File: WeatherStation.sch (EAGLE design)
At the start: 35 parts, among them J1 EDISON_CONNECTOR_FULLMOUNTING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, J2 EDISON_CONNECTOR_FULLHEADER, U1 MCP73831, U2 HTU21DSMD, U3 MPL3115A2LGA8, U4 PCA9306

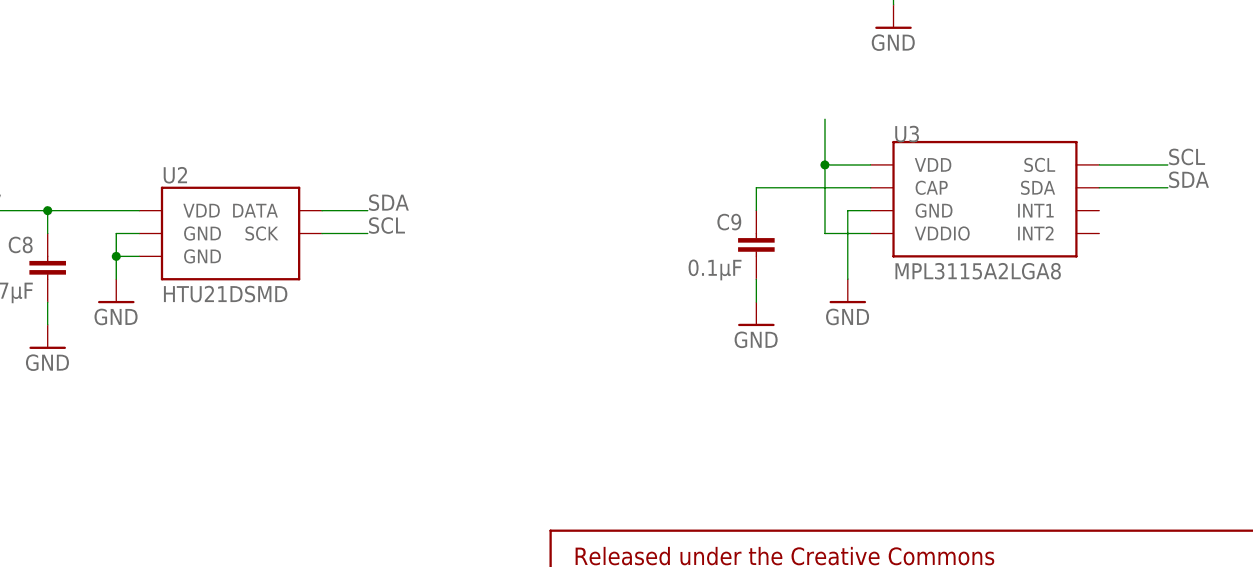
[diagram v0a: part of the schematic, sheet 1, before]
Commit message: rearranged silkscreens/labels
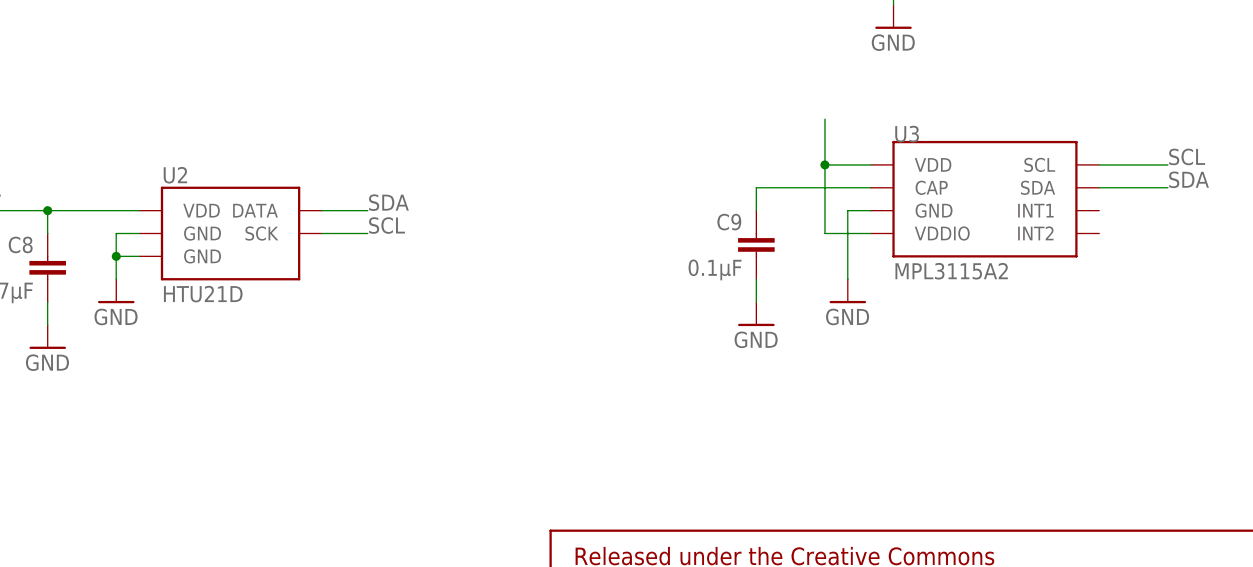
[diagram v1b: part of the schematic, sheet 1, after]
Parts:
- U2: value HTU21DSMD -> HTU21D
- U3: value MPL3115A2LGA8 -> MPL3115A2
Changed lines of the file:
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@@
 <part name="JP2" library="SparkFun-Connectors" deviceset="M02" device="PTH"/>
 <part name="GND8" library="SparkFun-Aesthetics" deviceset="GND" device=""/>
-<part name="U2" library="SparkFun-Sensors" deviceset="HTU21D" device="SMD"/>
-<part name="U3" library="SparkFun-Sensors" deviceset="MPL3115A2" device="LGA8"/>
+<part name="U2" library="SparkFun-Sensors" deviceset="HTU21D" device="SMD" value="HTU21D"/>
+<part name="U3" library="SparkFun-Sensors" deviceset="MPL3115A2" device="LGA8" value="MPL3115A2"/>
 <part name="U4" library="SparkFun-DigitalIC" deviceset="PCA9306" device="" value="PCA9306"/>
 <part name="U$1" library="SparkFun-PowerIC" deviceset="V_REG_MIC5205" device="3.3V" value="MIC5205"/>

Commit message: corrected values
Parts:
- C11, C8: value 4.7µF -> 0.1µF
- C3, C4: value 4.7µF -> 2.2µF
- C5: value 4.7µF -> 470pF
- R2: value 330Ω -> 470Ω
- R5: value 1kΩ -> 200kΩ
